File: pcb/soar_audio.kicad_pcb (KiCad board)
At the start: 2 copper layers, 100 x 98 mm, 116 parts, among them J1 RJ45-FLAPS, J2 RJ12-FLAPS, J3 RJ45-LED, J4 Screw_Terminal_01x02, J5 RJ45-CAN, J6 RJ12-I2C, J7 STM32F4_Discovery_Header, Q1 AO3401A, U1 LV2842X, U2 LV2842X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

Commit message: updated schematic and layout
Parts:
- removed C10: 10u, Capacitor_SMD:C_0805_2012Metric
- removed C23, C24, C25: 10n, Capacitor_SMD:C_0603_1608Metric
- removed C8: 100n, Capacitor_SMD:C_0603_1608Metric
- removed D10, D11, D18, D19, D20, D7, D8, D9: D_TVS, Diode_SMD:D_SOD-323
- removed FB2: Ferrite, Inductor_SMD:L_0805_2012Metric
- removed J7: STM32F4_Discovery_Header, STM32F4Di:stm32f4_discovery_header
- removed L2: 10u, Inductor_SMD:L_Bourns-SRN4018
- removed U2: LV2842X, Package_TO_SOT_SMD:TSOT-23-6
- removed U5: HAMMOND_1593W, OWN_PARTS:HAMMOND_1593W_edge_cut_notallmountingholes
- added JP5: Jumper_Open, Jumper:SolderJumper-2_P1.3mm_Open_Pad1.0x1.5mm, F.Cu at (156.3, 72.3)
- added R46: 4k7, Resistor_SMD:R_0603_1608Metric, F.Cu at (206.2, 139.3)
- added R47: 10k, Resistor_SMD:R_0603_1608Metric, F.Cu at (157.0, 75.1)
- C3: value 10u -> 100n; footprint Capacitor_SMD:C_0805_2012Metric -> Capacitor_SMD:C_0603_1608Metric
- C5: value 2u2 -> 10n; footprint Capacitor_SMD:C_0805_2012Metric -> Capacitor_SMD:C_0603_1608Metric
- D4: value D_B5819W -> D_TVS; footprint Diode_SMD:D_SOD-123 -> Diode_SMD:D_SOD-323
- J3: value RJ45-LED -> HEADER_4; footprint Connector_RJ:RJ45_Amphenol_RJHSE5380 -> Connector_PinHeader_1.27mm:PinHeader_1x04_P1.27mm_Vertical
- J6: value RJ12-I2C -> HEADER_4; footprint Connector_RJ:RJ12_Amphenol_54601 -> Connector_PinHeader_1.27mm:PinHeader_1x04_P1.27mm_Vertical
- R35: value 1k -> 120k; footprint Resistor_SMD:R_0805_2012Metric -> Resistor_SMD:R_0603_1608Metric
- R36: value 1k -> 120k
- R37: value 100k -> 56k
- R38: value 1k -> 30k; footprint Resistor_SMD:R_0805_2012Metric -> Resistor_SMD:R_0603_1608Metric
- R39: value 1k -> 15k
- R40: value 100k -> 7k5
- R41: value 1k -> 3k6; footprint Resistor_SMD:R_0805_2012Metric -> Resistor_SMD:R_0603_1608Metric
- R42: value 1k -> 1k8
- R43: value 100k -> 4k7
- R7: value 33k2 -> 1k; footprint Resistor_SMD:R_0603_1608Metric -> Resistor_SMD:R_0805_2012Metric
- R8: value 10k -> 1k
- moved J6 137.6 mm to (208.7, 146.2), turned to 0 degrees
- moved JP4 127.5 mm to (205.4, 149.9), turned to 0 degrees
- moved R8 125.8 mm to (156.7, 109.0)
- moved R7 125.2 mm to (159.9, 109.0), turned to 180 degrees
- moved JP3 124.4 mm to (205.3, 147.1), turned to 180 degrees
- moved R16 118.5 mm to (205.5, 152.1), turned to 0 degrees
- moved D6 118.5 mm to (201.9, 149.9), turned to 0 degrees
- moved D4 116.5 mm to (159.0, 111.8), turned to 90 degrees
- moved R15 114.0 mm to (205.4, 144.8), turned to 0 degrees
- moved D5 108.9 mm to (201.9, 147.1), turned to 0 degrees
- moved C5 106.4 mm to (157.0, 111.5), turned to 90 degrees
- moved R41 86.5 mm to (151.9, 80.6)
- moved R42 83.3 mm to (150.4, 80.6)
- moved R40 83.3 mm to (153.4, 80.6)
- moved C3 82.0 mm to (140.0, 63.8), turned to 90 degrees
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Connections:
- net ADCInput renamed ADC_Input1
- C22 pad 2: Flaps_In8 -> Flaps_In7
- C26 pad 2: ADCIn -> ADC_In1
- C3 pad 1: Net-(C3-Pad1) -> GND
- C3 pad 2: GND -> Net-(C2-Pad1)
- C5 pad 1: Net-(C3-Pad1) -> GND
- C5 pad 2: GND -> ADC_In2
- D4 pad 1: Net-(C8-Pad1) -> GND
- D4 pad 2: GND -> Net-(D4-Pad2)
- J2 pad 3: Switch_Gear_Input -> ADC_Input2
- J2 pad 4: Switch_AirBrakes_Input -> Flaps_Input6
- J2 pad 5: Switch_Flaps_Above_Neutral_Input -> Flaps_Input7
- J3 pad 1: +3V3 -> GND
- J3 pad 2: Shift_Reg_Neg_OE -> +3V3
- J3 pad 3: Shift_Reg_RCLK -> SCL2
- J3 pad 4: Shift_Reg_Neg_SRCLK -> SDA2
- J6 pad 1: +3V3 -> GND
- J6 pad 2: unconnected-(J6-Pad2) -> +3V3
- R33 pad 2: Flaps_In8 -> Flaps_In7
- R34 pad 1: Flaps_In8 -> Flaps_In7
- R35 pad 1: Switch_Gear_Input -> AIN+
- R35 pad 2: Net-(D18-Pad2) -> PWM_A
- R36 pad 1: Net-(D18-Pad2) -> PWM_B
- R36 pad 2: Switch_Gear_In -> AIN+
- R37 pad 1: Switch_Gear_In -> AIN+
- R37 pad 2: +3V3 -> ATTN_1
- R38 pad 1: Switch_AirBrakes_Input -> AIN+
- R38 pad 2: Net-(D19-Pad2) -> ATTN_2
- R39 pad 1: Net-(D19-Pad2) -> AIN+
- R39 pad 2: Switch_AirBrakes_In -> ATTN_3
- R40 pad 1: Switch_AirBrakes_In -> AIN+
- R40 pad 2: +3V3 -> ATTN_4
- R41 pad 1: Switch_Flaps_Above_Neutral_Input -> AIN+
- R41 pad 2: Net-(D20-Pad2) -> ATTN_5
- R42 pad 1: Net-(D20-Pad2) -> AIN+
- R42 pad 2: Switch_Flaps_Above_Neutral_In -> ATTN_6
- R43 pad 1: Switch_Flaps_Above_Neutral_In -> +3V3
- R43 pad 2: +3V3 -> SCL2
- R45 pad 2: ADCIn -> ADC_In1
- R7 pad 1: +3V3 -> ADC_Input2
- R7 pad 2: Net-(R7-Pad2) -> Net-(D4-Pad2)
- R8 pad 1: Net-(R7-Pad2) -> Net-(D4-Pad2)
- R8 pad 2: GND -> ADC_In2
- U6 pad 3V3: unconnected-(U6-Pad3V3) -> +3V3
- U6 pad 5V: unconnected-(U6-Pad5V) -> +5V
- U6 pad G: unconnected-(U6-PadG) -> GND
- U6 pad PA0: unconnected-(U6-PadPA0) -> PWM_A
- U6 pad PA1: unconnected-(U6-PadPA1) -> PWM_B
- U6 pad PA10: unconnected-(U6-PadPA10) -> Flaps_In7
- U6 pad PA2: unconnected-(U6-PadPA2) -> ATTN_1
- U6 pad PA3: unconnected-(U6-PadPA3) -> ATTN_2
- U6 pad PA4: unconnected-(U6-PadPA4) -> ATTN_3
- U6 pad PA5: unconnected-(U6-PadPA5) -> ATTN_4
- U6 pad PA6: unconnected-(U6-PadPA6) -> ATTN_5
- U6 pad PA7: unconnected-(U6-PadPA7) -> ATTN_6
- U6 pad PA8: unconnected-(U6-PadPA8) -> Flaps_In5
- U6 pad PA9: unconnected-(U6-PadPA9) -> Flaps_In6
- U6 pad PB0: unconnected-(U6-PadPB0) -> ADC_In1
- U6 pad PB1: unconnected-(U6-PadPB1) -> ADC_In2
- U6 pad PB10: unconnected-(U6-PadPB10) -> SCL2
- U6 pad PB11: unconnected-(U6-PadPB11) -> SDA2
- U6 pad PB12: unconnected-(U6-PadPB12) -> Flaps_In1
- U6 pad PB13: unconnected-(U6-PadPB13) -> Flaps_In2
- U6 pad PB14: unconnected-(U6-PadPB14) -> Flaps_In3
- U6 pad PB15: unconnected-(U6-PadPB15) -> Flaps_In4
- U6 pad PB6: unconnected-(U6-PadPB6) -> SCL
- U6 pad PB7: unconnected-(U6-PadPB7) -> SDA
- U6 pad PB8: unconnected-(U6-PadPB8) -> CAN_RX
- U6 pad PB9: unconnected-(U6-PadPB9) -> CAN_TX
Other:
- board outline removed

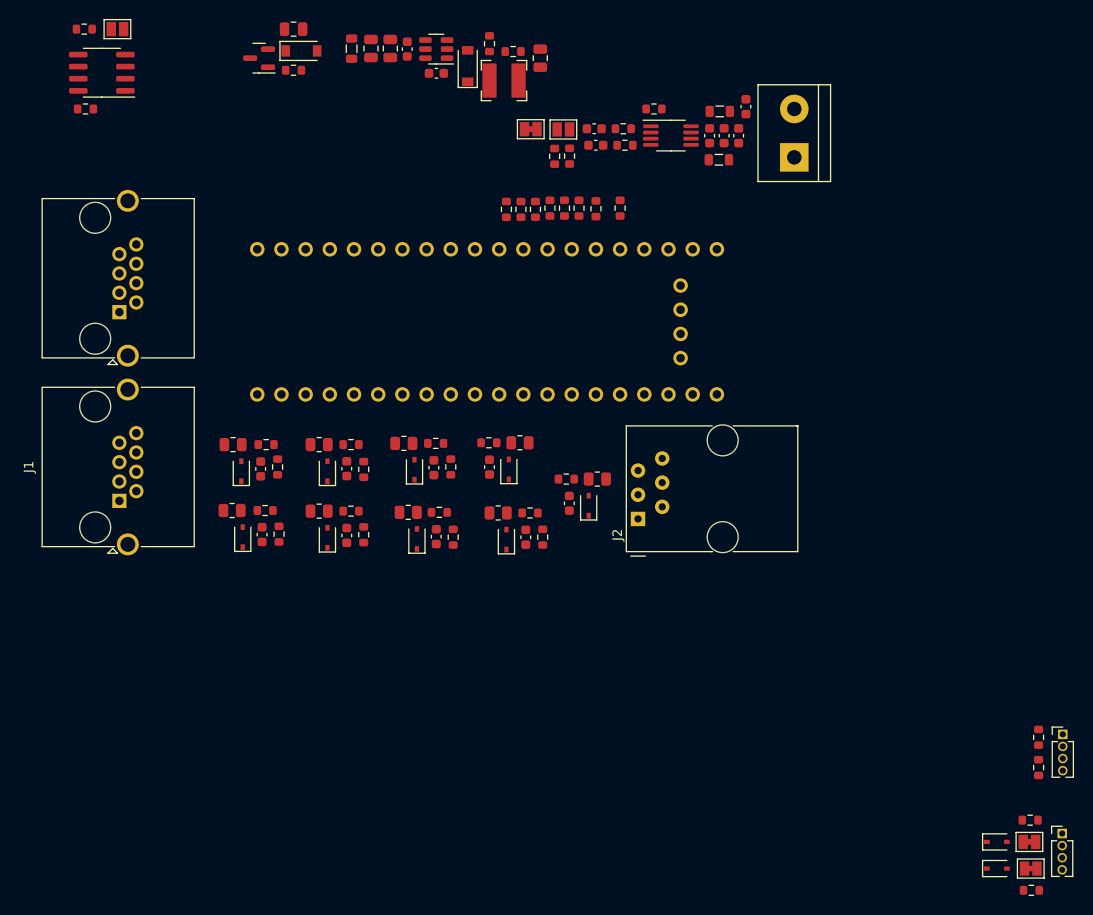
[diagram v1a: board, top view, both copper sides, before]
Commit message: updated jlc rules to layout
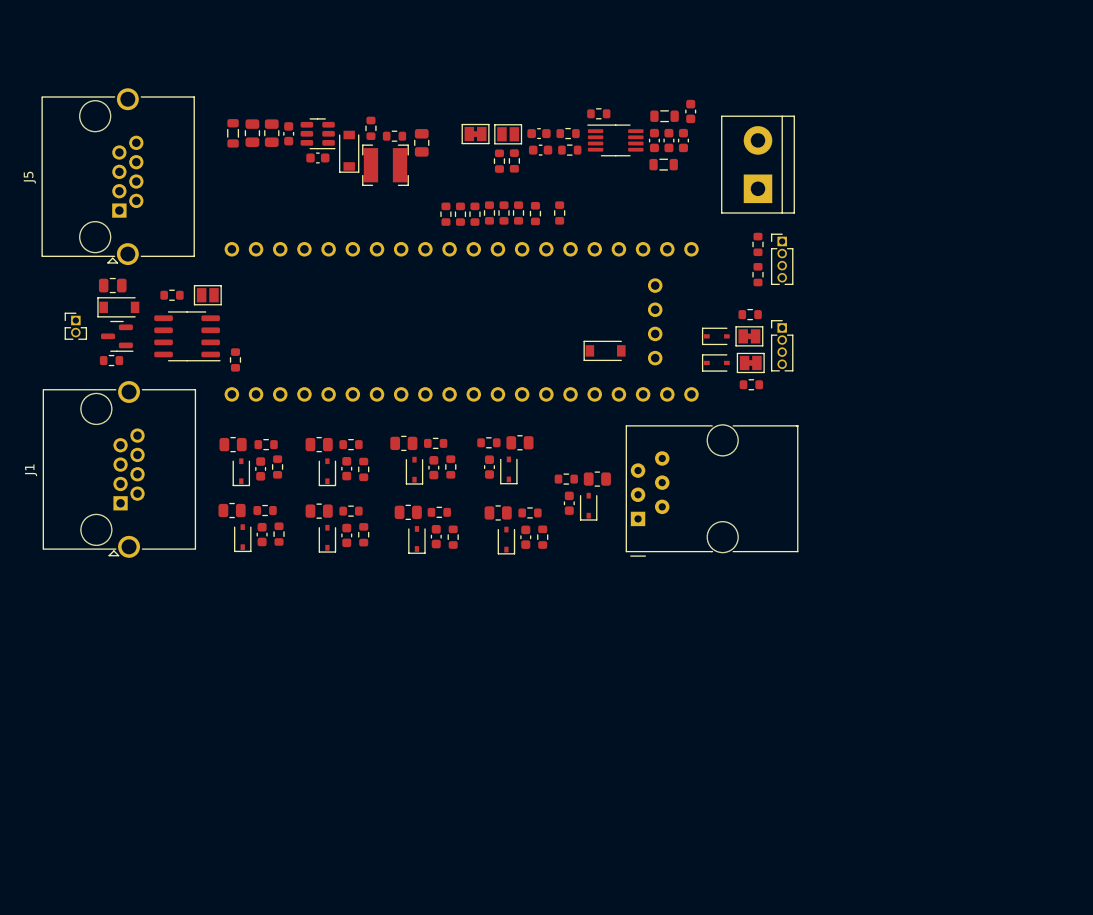
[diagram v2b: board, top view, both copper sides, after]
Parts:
- added D7: D_B5819W, Diode_SMD:D_SOD-123, F.Cu at (160.8, 95.5)
- added J7: HEADER_2, Connector_PinHeader_1.27mm:PinHeader_1x02_P1.27mm_Vertical, F.Cu at (105.2, 92.3)
- moved JP4 60.7 mm to (176.0, 96.8)
- moved D5 60.7 mm to (172.5, 94.0)
- moved D6 60.7 mm to (172.5, 96.8)
- moved JP3 60.7 mm to (175.9, 94.0)
- moved R15 60.7 mm to (176.0, 91.7)
- moved J6 60.7 mm to (179.3, 93.1)
- moved R16 60.7 mm to (176.1, 99.1)
- moved J3 59.6 mm to (179.3, 84.0)
- moved R46 59.6 mm to (176.8, 87.5)
- moved R43 59.6 mm to (176.8, 84.3)
- moved R1 36.0 mm to (108.9, 96.5)
- moved D1 33.0 mm to (109.7, 90.9)
- moved C1 32.9 mm to (109.0, 88.6)
- moved Q1 32.8 mm to (109.5, 94.0)
- moved R10 30.7 mm to (121.9, 96.5), turned to -90 degrees
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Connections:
- U6 pad 5V: +5V -> Net-(U6-Pad5V)
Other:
- copper layers 2 -> 4

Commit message: some more steps done
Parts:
- moved R28 11.7 mm to (144.5, 107.4)
- moved D15 11.7 mm to (140.7, 107.8)
- moved R26 11.7 mm to (139.9, 105.0)
- moved R27 11.7 mm to (143.2, 105.0)
- moved C20 11.7 mm to (142.7, 107.5)
- moved D12 11.4 mm to (131.6, 114.8)
- moved R17 11.4 mm to (130.5, 112.1)
- moved R18 11.4 mm to (133.8, 112.1)
- moved R19 11.4 mm to (135.4, 114.6)
- moved C17 11.4 mm to (133.6, 114.6)
- moved C21 9.40 mm to (143.0, 114.8)
- moved D16 9.40 mm to (141.0, 115.1)
- moved R29 9.40 mm to (140.1, 112.3)
- moved R30 9.40 mm to (143.4, 112.3)
- moved R31 9.40 mm to (144.8, 114.8)
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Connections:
- U6 pad VBAT: unconnected-(U6-PadVBAT) -> +3V3
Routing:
- net GND: track 0.00 -> 72.7 mm, vias 0 -> 17
- net +5V: track 0.00 -> 72.0 mm
- net Flaps_Input6: track 0.00 -> 62.5 mm, vias 0 -> 1
- net Flaps_Input7: track 0.00 -> 62.1 mm, vias 0 -> 1
- net SCL2: track 0.00 -> 55.1 mm
- net SDA2: track 0.00 -> 53.1 mm
- net CAN_RX: track 0.00 -> 52.9 mm
- net CAN_TX: track 0.00 -> 44.6 mm
- net VSUPPLY: track 0.00 -> 38.8 mm
- net ADC_In2: track 0.00 -> 38.5 mm, vias 0 -> 1
- net Flaps_Input5: track 0.00 -> 37.5 mm, vias 0 -> 1
- net Flaps_Input3: track 0.00 -> 35.3 mm, vias 0 -> 1
- net SCL: track 0.00 -> 33.2 mm
- net Flaps_In7: track 0.00 -> 32.3 mm
- net ADC_In1: track 0.00 -> 29.2 mm, vias 0 -> 1
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- added copper zone on In2.Cu, net +3V3
- added copper zone on In1.Cu, net GND
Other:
- board outline added: 79 x 51 mm

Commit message: add toolingholes
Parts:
- added C10: 100n, Capacitor_SMD:C_0603_1608Metric, F.Cu at (134.1, 78.5)
- added C8: 1u, Capacitor_SMD:C_0603_1608Metric, F.Cu at (134.1, 80.0)
- added J8: HEADER_4, Connector_PinHeader_2.54mm:PinHeader_1x04_P2.54mm_Vertical, F.Cu at (139.7, 69.9)
- added J9: HEADER_4, Connector_PinHeader_2.54mm:PinHeader_1x04_P2.54mm_Vertical, F.Cu at (143.5, 69.9)
- moved R5 14.1 mm to (126.0, 69.4), turned to -90 degrees
- moved R6 9.43 mm to (127.5, 69.5), turned to 90 degrees
- moved C9 7.91 mm to (134.2, 76.7), turned to 180 degrees
- moved C7 5.63 mm to (133.3, 70.4), turned to 180 degrees
- moved J6 5.09 mm to (178.8, 98.2)
- moved JP4 4.57 mm to (175.4, 101.3)
- moved JP3 4.57 mm to (175.4, 98.6)
- moved D3 4.42 mm to (129.5, 75.4), turned to 180 degrees
- moved R15 4.27 mm to (176.8, 95.2), turned to -90 degrees
- moved R16 4.19 mm to (178.8, 95.2), turned to -90 degrees
- moved L1 4.01 mm to (134.6, 73.4)
- moved D6 3.59 mm to (172.5, 100.3), turned to -90 degrees
- moved D5 3.07 mm to (174.8, 95.2), turned to -90 degrees
- moved U1 0.77 mm to (130.0, 72.1), turned to -90 degrees
- moved J4 0.36 mm to (176.3, 75.7)
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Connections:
- J1 pad 1: Flaps_Input1 -> GND
- J1 pad 8: GND -> Flaps_Input1
- J2 pad 1: +3V3 -> GND
- J2 pad 6: GND -> +3V3
- J5 pad 1: VSUPPLY_IN -> GND
- J5 pad 2: VSUPPLY_IN -> GND
- J5 pad 7: GND -> VSUPPLY_IN
- J5 pad 8: GND -> VSUPPLY_IN
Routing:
- net +5V: track 72.0 -> 96.8 mm
- net GND: track 72.7 -> 90.2 mm, vias 17 -> 21
- net Flaps_Input1: track 28.0 -> 13.0 mm
- net Net-(R5-Pad2): track 9.22 -> 3.43 mm
- net SDA: track 28.6 -> 34.0 mm
- net VSUPPLY_IN: track 25.3 -> 30.6 mm
- net Net-(C15-Pad1): track 11.0 -> 14.4 mm
- net Net-(C16-Pad1): track 9.42 -> 12.4 mm
- net +3V3: track 17.9 -> 20.0 mm, vias 13 -> 11
- net VSUPPLY: track 38.8 -> 40.3 mm
- net Net-(C7-Pad1): track 9.39 -> 7.93 mm
- net Net-(C2-Pad1): track 8.91 -> 9.80 mm
- net Net-(D5-Pad2): track 1.71 -> 2.26 mm
- net Net-(FB4-Pad1): track 2.60 -> 3.14 mm
- net SDA2: track 53.1 -> 52.6 mm
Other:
- outline, holes or cut-outs redrawn
- board text added: "JLCJLCJLCJLC"

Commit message: finalized pcb
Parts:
- moved D6 5.08 mm to (172.5, 95.2)
- moved R46 1.28 mm to (174.8, 83.2)
- moved JP3 1.27 mm to (174.1, 98.6)
- moved JP4 1.27 mm to (174.1, 101.3)
- moved R43 1.27 mm to (174.8, 80.2)
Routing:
- net Net-(D6-Pad2): track 2.27 -> 6.45 mm
- net SCL: track 33.7 -> 31.0 mm
- net +3V3: track 20.0 -> 17.4 mm, vias 11 -> 12
- net SDA: track 34.0 -> 35.4 mm
- net SCL2: track 55.1 -> 56.4 mm
- net GND: track 90.2 -> 91.5 mm
- net SDA2: track 52.6 -> 53.8 mm
- net Net-(D5-Pad2): track 2.26 -> 2.79 mm
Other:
- board text added: "+"
- board text added: "-"
- board text added: "3V3"
- board text added: "4 - 8 Ohm"
- board text added: "5V"
- board text added: "C"
- board text added: "CAN"
- board text added: "D"
- board text added: "FLAPS"
- board text added: "I2C"
- board text added: "I2C2"
- board text added: "Maximilian Betz"
- board text added: "SOAR UTILITY"
- board text added: "pcbDesign:"
- board text added: "the"
- board text added: "v1.0 2022-01-05"
